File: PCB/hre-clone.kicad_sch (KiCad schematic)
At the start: 23 parts, among them SW1 SW_DIP_x04, U1 74LS258, U10 MC6845, U11 MC6845, U12 DIL14, U13 7402, U2 74LS174, U3 74LS257, U4 74LS244, U5 2716, U6 2716, U7 74LS05, U8 74LS155, U9 74LS257

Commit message: Re-organize file, remove backup files, update readme
A little more organization always helps!
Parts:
- U1, U2, U3, U8, U9: footprint Housings_DIP:DIP-16_W7.62mm_LongPads -> Package_DIP:DIP-16_W7.62mm
- U12, U13, U7: footprint Housings_DIP:DIP-14_W7.62mm_LongPads -> Package_DIP:DIP-14_W7.62mm
- U4: footprint Housings_DIP:DIP-20_W7.62mm_LongPads -> Package_DIP:DIP-20_W7.62mm
- U5, U6: footprint Housings_DIP:DIP-24_W15.24mm_LongPads -> Package_DIP:DIP-24_W15.24mm
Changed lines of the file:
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@@
 			)
 		)
-		(property "Footprint" "Housings_DIP:DIP-16_W7.62mm_LongPads"
+		(property "Footprint" "Package_DIP:DIP-16_W7.62mm"
 			(at 128.27 61.214 0)
 			(hide yes)
@@
 			)
 		)
-		(property "Footprint" "Housings_DIP:DIP-16_W7.62mm_LongPads"
+		(property "Footprint" "Package_DIP:DIP-16_W7.62mm"
 			(at 189.23 58.166 0)
 			(hide yes)
@@
 			)
 		)
-		(property "Footprint" "Housings_DIP:DIP-16_W7.62mm_LongPads"
+		(property "Footprint" "Package_DIP:DIP-16_W7.62mm"
 			(at 260.604 58.674 0)
 			(hide yes)
@@
 			)
 		)
-		(property "Footprint" "Housings_DIP:DIP-20_W7.62mm_LongPads"
+		(property "Footprint" "Package_DIP:DIP-20_W7.62mm"
 			(at 48.514 58.928 0)
 			(hide yes)
@@
 			)
 		)
-		(property "Footprint" "Housings_DIP:DIP-24_W15.24mm_LongPads"
+		(property "Footprint" "Package_DIP:DIP-24_W15.24mm"
 			(at 80.518 109.22 0)
 			(hide yes)
@@
 			)
 		)
-		(property "Footprint" "Housings_DIP:DIP-24_W15.24mm_LongPads"
+		(property "Footprint" "Package_DIP:DIP-24_W15.24mm"
 			(at 144.526 108.458 0)
 			(hide yes)
@@
 			)
 		)
-		(property "Footprint" "Housings_DIP:DIP-14_W7.62mm_LongPads"
+		(property "Footprint" "Package_DIP:DIP-14_W7.62mm"
 			(at 190.754 91.186 0)
 			(hide yes)
@@
 			)
 		)
-		(property "Footprint" "Housings_DIP:DIP-14_W7.62mm_LongPads"
+		(property "Footprint" "Package_DIP:DIP-14_W7.62mm"
 			(at 190.754 101.346 0)
 			(hide yes)
@@
 			)
 		)
-		(property "Footprint" "Housings_DIP:DIP-14_W7.62mm_LongPads"
+		(property "Footprint" "Package_DIP:DIP-14_W7.62mm"
 			(at 190.754 111.506 0)
 			(hide yes)
@@
 			)
 		)
-		(property "Footprint" "Housings_DIP:DIP-14_W7.62mm_LongPads"
+		(property "Footprint" "Package_DIP:DIP-14_W7.62mm"
 			(at 190.754 121.666 0)
 			(hide yes)
@@
 			)
 		)
-		(property "Footprint" "Housings_DIP:DIP-14_W7.62mm_LongPads"
+		(property "Footprint" "Package_DIP:DIP-14_W7.62mm"
 			(at 190.754 130.556 0)
 			(hide yes)
@@
 			)
 		)
-		(property "Footprint" "Housings_DIP:DIP-14_W7.62mm_LongPads"
+		(property "Footprint" "Package_DIP:DIP-14_W7.62mm"
 			(at 190.754 139.446 0)
 			(hide yes)
@@
 			)
 		)
-		(property "Footprint" "Housings_DIP:DIP-16_W7.62mm_LongPads"
+		(property "Footprint" "Package_DIP:DIP-16_W7.62mm"
 			(at 262.128 95.504 0)
 			(hide yes)
@@
 			)
 		)
-		(property "Footprint" "Housings_DIP:DIP-16_W7.62mm_LongPads"
+		(property "Footprint" "Package_DIP:DIP-16_W7.62mm"
 			(at 256.794 129.286 0)
 			(hide yes)
@@
 			)
 		)
-		(property "Footprint" "Housings_DIP:DIP-14_W7.62mm_LongPads"
+		(property "Footprint" "Package_DIP:DIP-14_W7.62mm"
 			(at 251.46 159.258 0)
 			(hide yes)
@@
 			)
 		)
-		(property "Footprint" "Housings_DIP:DIP-14_W7.62mm_LongPads"
+		(property "Footprint" "Package_DIP:DIP-14_W7.62mm"
 			(at 251.46 171.958 0)
 			(hide yes)
@@
 			)
 		)
-		(property "Footprint" "Housings_DIP:DIP-14_W7.62mm_LongPads"
+		(property "Footprint" "Package_DIP:DIP-14_W7.62mm"
 			(at 251.714 186.944 0)
 			(hide yes)
@@
 			)
 		)
-		(property "Footprint" "Housings_DIP:DIP-14_W7.62mm_LongPads"
+		(property "Footprint" "Package_DIP:DIP-14_W7.62mm"
 			(at 251.714 200.914 0)
 			(hide yes)
@@
 			)
 		)
-		(property "Footprint" "Housings_DIP:DIP-14_W7.62mm_LongPads"
+		(property "Footprint" "Package_DIP:DIP-14_W7.62mm"
 			(at 189.23 181.102 0)
 			(hide yes)

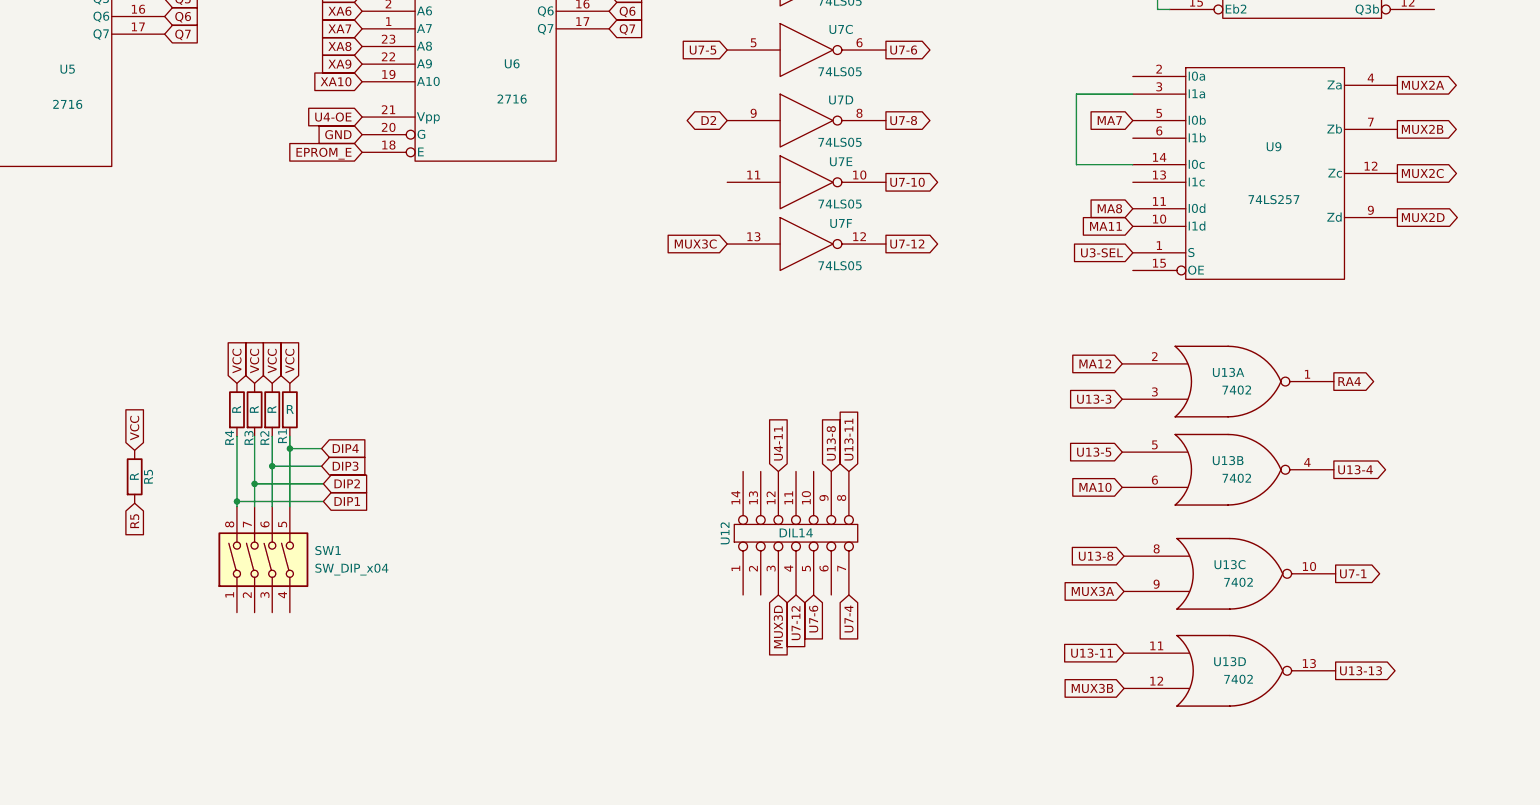
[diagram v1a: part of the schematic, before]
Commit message: Some additional PCB fixes
Getting closer to complete routing. Still some traces under chips that can not be determined.
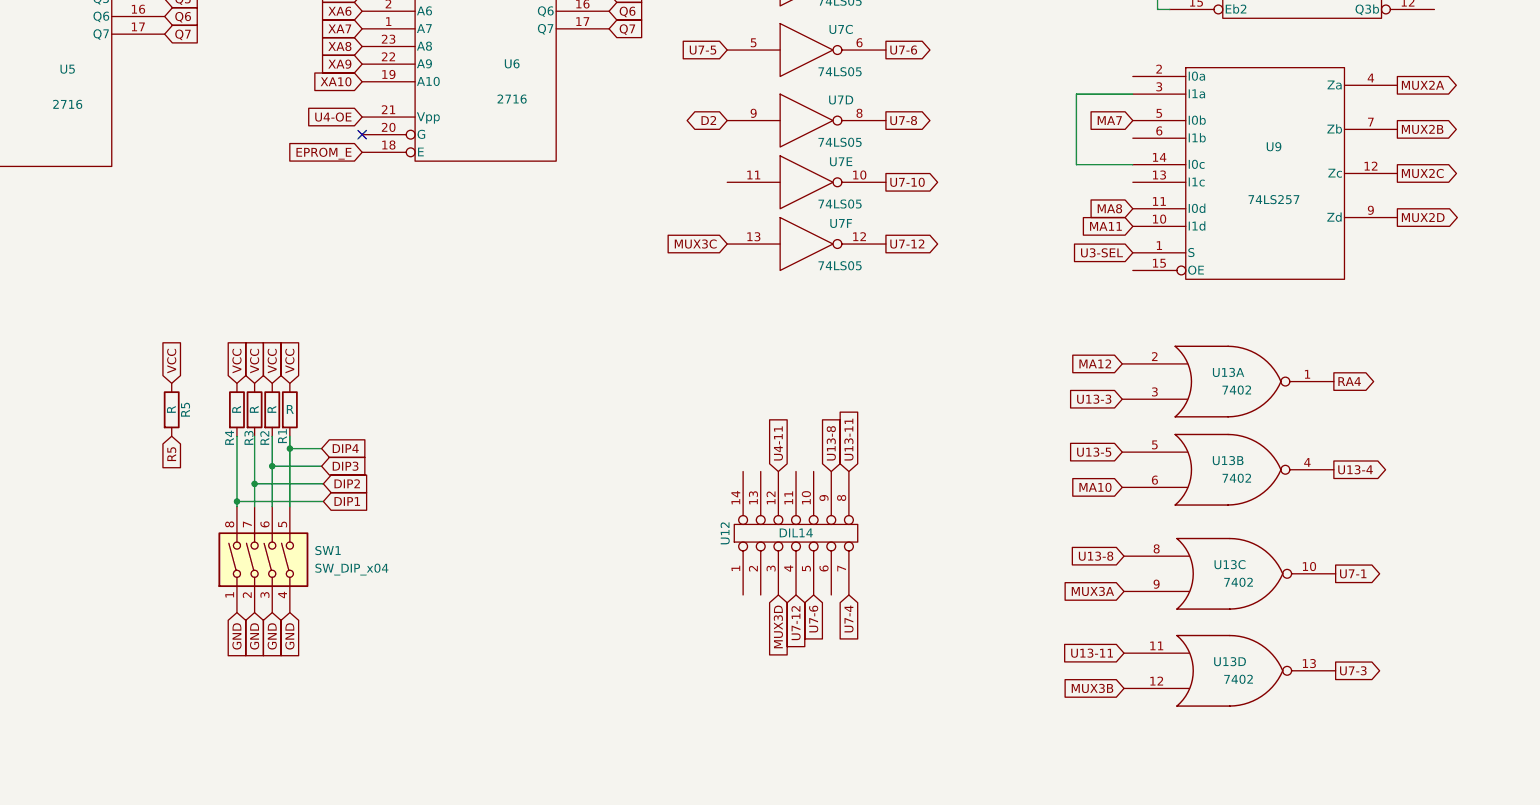
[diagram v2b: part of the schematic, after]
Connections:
- net U13-13 is gone; now on net U7-3: U13.13
- net GND: now also SW1.1, SW1.2, SW1.3, SW1.4; no longer U6.20 (G)
- no-connect marks 0 -> 1
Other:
- moved on the sheet: R5
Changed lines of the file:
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@@
 		(color 0 0 0 0)
 	)
+	(no_connect
+		(at 126.746 123.698)
+	)
 	(wire
 		(pts
@@
 		)
 	)
-	(global_label "U13-13"
+	(global_label "U7-3"
 		(shape output)
 		(at 266.954 200.914 0)
@@
 		)
 		(property "Intersheetrefs" "${INTERSHEET_REFS}"
-			(at 277.0259 200.914 0)
+			(at 274.6069 200.914 0)
 			(hide yes)
 			(show_name no)
@@
 		)
 	)
+	(global_label "GND"
+		(shape input)
+		(at 111.252 192.532 270)
+		(fields_autoplaced yes)
+		(effects
+			(font
+				(size 1.27 1.27)
+			)
+			(justify right)
+		)
+		(property "Intersheetrefs" "${INTERSHEET_REFS}"
+			(at 111.252 198.7335 90)
+			(hide yes)
+			(show_name no)
+			(do_not_autoplace no)
+			(effects
+				(font
+					(size 1.27 1.27)
+				)
+				(justify right)
+			)
+		)
+	)
 	(global_label "D2"
 		(shape bidirectional)
@@
 		)
 	)
+	(global_label "GND"
+		(shape input)
+		(at 113.792 192.532 270)
+		(fields_autoplaced yes)
+		(effects
+			(font
+				(size 1.27 1.27)
+			)
+			(justify right)
+		)
+		(property "Intersheetrefs" "${INTERSHEET_REFS}"
+			(at 113.792 198.7335 90)
+			(hide yes)
+			(show_name no)
+			(do_not_autoplace no)
+			(effects
+				(font
+					(size 1.27 1.27)
+				)
+				(justify right)
+			)
+		)
+	)
 	(global_label "MUX3D"
 		(shape output)
@@
 		)
 	)
+	(global_label "GND"
+		(shape input)
+		(at 116.332 192.532 270)
+		(fields_autoplaced yes)
+		(effects
+			(font
+				(size 1.27 1.27)
+			)
+			(justify right)
+		)
+		(property "Intersheetrefs" "${INTERSHEET_REFS}"
+			(at 116.332 198.7335 90)
+			(hide yes)
+			(show_name no)
+			(do_not_autoplace no)
+			(effects
+				(font
+					(size 1.27 1.27)
+				)
+				(justify right)
+			)
+		)
+	)
 	(global_label "MUX1B"
 		(shape input)
@@
 	(global_label "VCC"
 		(shape input)
-		(at 93.98 169.164 90)
+		(at 99.314 159.512 90)
 		(fields_autoplaced yes)
 		(effects
@@
 		)
 		(property "Intersheetrefs" "${INTERSHEET_REFS}"
-			(at 93.98 163.2044 90)
+			(at 99.314 153.5524 90)
 			(hide yes)
 			(show_name no)
@@
 	(global_label "R5"
 		(shape input)
-		(at 93.98 176.784 270)
+		(at 99.314 167.132 270)
 		(fields_autoplaced yes)
 		(effects
@@
 		)
 		(property "Intersheetrefs" "${INTERSHEET_REFS}"
-			(at 93.98 181.5945 90)
+			(at 99.314 171.9425 90)
 			(hide yes)
 			(show_name no)
@@
 		)
 	)
-	(global_label "GND"
-		(shape input)
-		(at 126.746 123.698 180)
-		(fields_autoplaced yes)
-		(effects
-			(font
-				(size 1.27 1.27)
-			)
-			(justify right)
-		)
-		(property "Intersheetrefs" "${INTERSHEET_REFS}"
-			(at 120.5445 123.698 0)
-			(hide yes)
-			(show_name no)
-			(do_not_autoplace no)
-			(effects
-				(font
-					(size 1.27 1.27)
-				)
-				(justify right)
-			)
-		)
-	)
 	(global_label "RA2"
 		(shape input)
@@
 		)
 	)
+	(global_label "GND"
+		(shape input)
+		(at 108.712 192.532 270)
+		(fields_autoplaced yes)
+		(effects
+			(font
+				(size 1.27 1.27)
+			)
+			(justify right)
+		)
+		(property "Intersheetrefs" "${INTERSHEET_REFS}"
+			(at 108.712 198.7335 90)
+			(hide yes)
+			(show_name no)
+			(do_not_autoplace no)
+			(effects
+				(font
+					(size 1.27 1.27)
+				)
+				(justify right)
+			)
+		)
+	)
 	(global_label "D1"
 		(shape bidirectional)
@@
 	(symbol
 		(lib_id "Device:R")
-		(at 93.98 172.974 0)
+		(at 99.314 163.322 0)
 		(unit 1)
 		(body_style 1)
@@
 		(dnp no)
 		(property "Reference" "R5"
-			(at 96.012 172.974 90)
+			(at 101.346 163.322 90)
 			(show_name no)
 			(do_not_autoplace no)
@@
 		)
 		(property "Value" "R"
-			(at 93.98 172.974 90)
+			(at 99.314 163.322 90)
 			(show_name no)
 			(do_not_autoplace no)
@@
 		)
 		(property "Footprint" "Resistor_THT:R_Axial_DIN0309_L9.0mm_D3.2mm_P12.70mm_Horizontal"
-			(at 92.202 172.974 90)
+			(at 97.536 163.322 90)
 			(hide yes)
 			(show_name no)
@@
 		)
 		(property "Datasheet" ""
-			(at 93.98 172.974 0)
+			(at 99.314 163.322 0)
 			(show_name no)
 			(do_not_autoplace no)
@@
 		)
 		(property "Description" ""
-			(at 93.98 172.974 0)
+			(at 99.314 163.322 0)
 			(show_name no)
 			(do_not_autoplace no)

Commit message: Updated schematics and routing
There are now zero unrouted connections, but a few remaining connections missing under the chips. Added a picture of the traces under the CRTC chip.
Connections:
- net U13-4 is gone; now on an unnamed net: U13.4
- net U13-5 is gone; now on net MA10: U13.5
- net U3-11 is gone; now on net RA2: U3.11 (I0d)
- net U3-13 is gone; now on net MA8: U3.13 (I1c)
- net U3-2 is gone; now on net RA0: U3.2 (I0a)
- net U3-5 is gone; now on net RA1: U3.5 (I0b)
- net U4-12 is gone; now on net Q0: U4.12 (O3a)
- net U4-14 is gone; now on net Q2: U4.14 (O2a)
- net U4-2 is gone; now on net XA7: U4.2 (I0a)
- net U4-3 is gone; now on net Q5: U4.3 (O3b)
- net U4-7 is gone; now on net Q1: U4.7 (O1b)
- net U4-8 is gone; now on net XA5: U4.8 (I3a)
- net U4-9 is gone; now on net XA3: U4.9 (O0b)
- net U4-OE is gone; now on net U3-SEL: U4.1 (OEa), U4.19 (OEb), U5.21 (Vpp), U6.21 (Vpp)
- net U7-8 is gone; now on net R5: U7.8
- net D3: no longer U2.11 (D3)
- net D4: now also U2.11 (D3); no longer U2.13 (D4)
- net D5: now also U2.13 (D4); no longer U2.14 (D5)
- net DIP1: now also U1.11 (I0d)
- net DIP2: now also U1.5 (I0b)
- net DIP3: now also U1.14 (I0c)
- net GND: now also U8.14 (Eb1), U8.15 (Eb2), U9.15 (OE)
- net MA6: now also U9.2 (I0a)
- net MA9: now also U9.6 (I1b); no longer U10.13 (MA9)
- net MUX2A: now also U10.13 (MA9)
- net RA4: no longer U11.34 (RA4)
- net U2-CP: no longer U2.9 (Cp)
- net U2-MR: no longer U2.1 (~{Mr})
- net ~{CS}: no longer U11.25 (~{CS})
- net U8-13: now reaches U8.13 (A0)
- net U8-13: now also U12.6
- net LATCH: now reaches U8.4 (Q3a)
- net LATCH: now also U2.9 (Cp)
- net RS renamed A0
- net A0: now also U2.14 (D5)
- net U13-3: no longer names the net of U13.3
- net U8-9 renamed ~{CRTC_CS}
- net ~{CRTC_CS}: now also U11.25 (~{CS})
- no-connect marks 1 -> 2
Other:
- note added: "$E880-$E881"
- note added: "$E882-$E883"
- note added: "8296 HRE Clone"
- note added: "Address Translation ??? ============ U10 U11 U11 TEXT HIRES MA5 MA5 RA0 MA6 MA6 RA1 MA7 MA7 RA2 MA8 MA8 MA5 MA9 MA9 MA6 MA10 MA10 MA7 MA11 MA11 MA8 MA12 MA12 MA9"
- note added: "CHAR ROM"
- note added: "CHAR ROM HEADER"
- note added: "CREATED: 2016-04-22 UPDATED: 2026-10-11"
- note added: "CRTC HEADER"
- note added: "DECODER"
- note added: "Emulates HSG Board"
- note added: "LATCH"
- note added: "MULTIPLEXERS"
- note added: "Missing Q2 and Q7"
- note added: "This is a clone of the Commodore 8296 High-Res Emulator (HRE) board. The HRE is a board plus firmware that emulates the Commodore High-Speed Grahic (HSG) board which contains a Thomson EF9365/EF9366 Video Display Processor (VDP). The HRE firmware implements the same BASIC commands as the HSG but does the drawing with the 6502 processor rather than the VDP chip."
- note added: "XCVR"
- note removed: "CREATED: 2016-04-22 UPDATED: 2026-10-10"
- note removed: "CRTC SOCKET"
- note removed: "High Res Emulator of HRG Board"
- note removed: "PET HRE Clone"
- note removed: "This is a clone of the Commodore 8296 High-Res Emulator (HRE) board. The HRE is a board plus firmware that emulates the Commodore High-Speed Grahic (HSG) board which contains a Thomson EF Video Display Processor (VDP). The HRE firmware implements the same BASIC commands as the HSG but does the drawing with the 6502 processor rather than the VDP chip."
- moved on the sheet: R1, R2, R3, R4, R5, SW1, U1, U10, U11, U12, U13A, U13B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

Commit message: Routing complete
Thanks to Andy Grady for corrections for some traces. DRC check ok. Updated many global labels, moved around some symbols, updated board text etc
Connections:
- net U3-SEL is gone; now on net MUX2SEL: U3.1 (S), U4.1 (OEa), U4.19 (OEb), U5.21 (Vpp), U6.21 (Vpp), U9.1 (S)
- net U4-17 is gone; now on net XA8: U4.17 (I3b)
- net U4-6 is gone; now on net XA5: U4.6 (I2a)
- net D7: now also U2.14 (D5)
- net GND: now also U9.13 (I1c)
- net LATCH: now also U8.6 (Q1a); no longer U8.4 (Q3a)
- net MA10: now also U9.6 (I1b)
- net MA9: now also U9.14 (I0c), U9.3 (I1a); no longer U9.6 (I1b)
- net Q7: now also U4.9 (O0b)
- net XA3: now also U4.8 (I3a); no longer U4.9 (O0b)
- net XA5: no longer U4.8 (I3a)
- net ~{RESET}: now also U2.1 (~{Mr})
- net RIBBON-11: now reaches U12.11
- net RIBBON-11: now also U8.13 (A0)
- net A0 renamed RS
- net RS: no longer U2.14 (D5)
- net EPROM_E renamed XA11
- net MA12 renamed MUX2SEL
- net MUX3C: no longer names the net of U1.12 (Zc), U7.13
- net R5: no longer names the net of R5.2, U2.6 (D2), U7.8
- net U1-10 renamed LATCH1
- net U1-3 renamed LATCH4
- net U1-6 renamed LATCH3
- net U1-SEL renamed MUX1SEL
- net U13-11 renamed RIBBON-8
- net U13-8 renamed RIBBON-9
- net U2-2 renamed LATCH0
- net U4-11 renamed RIBBON-12
- net U7-1: no longer names the net of U13.10, U7.1
- net U7-10: no longer names the net of U7.10
- net U7-12 renamed ~{MUX3C}
- net U7-3: no longer names the net of U13.13, U7.3
- net U7-4 renamed RIBBON-7
- net U7-5: no longer names the net of U2.7 (Q2), U7.5
- net U7-6 renamed ~{LATCH2}
- net U8-13: no longer names the net of U12.6
- net U8-13: no longer U8.13 (A0)
- no-connect marks 2 -> 16
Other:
- note added: "/CS"
- note added: "A11"
- note added: "Address Translation =================== U10 U11 U11 --- --- --- MODE: TEXT HIRES MA5 MA5 RA0 MA6 MA6 RA1 MA7 MA7 RA2 MA8 MA8 MA5 MA9 MA9 MA6 MA10 MA10 MA7 MA11 MA11 MA8 MA12 MA12 MA9"
- note added: "CREATED: 2016-04-22 UPDATED: 2026-10-12"
- note added: "DIP SWITCHES"
- note added: "RIBBON CABLE"
- note added: "SPARES"
- note added: "The CHR ROM socket supports a 2316 (2K) or 2332 (4K). Normally it is only 2K except for SuperPET or some DIN machines. * Pin 18 is used as A11. * Pin 21 is used as /CS"
- note added: "This is a clone of the Commodore 8296 High-Res Emulator (HRE) board. The HRE is a board plus firmware that emulates the Commodore High-Speed Grahic (HSG) board which contains a Thomson EF9365/EF9366 Video Display Processor (VDP). The HRE firmware implements the same BASIC commands as the HSG but does the drawing with the 6502 processor rather than the VDP chip. Thanks to Andy Grady for sorting ou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"
- note added: "To CHR ROM"
- note removed: "Address Translation ??? ============ U10 U11 U11 TEXT HIRES MA5 MA5 RA0 MA6 MA6 RA1 MA7 MA7 RA2 MA8 MA8 MA5 MA9 MA9 MA6 MA10 MA10 MA7 MA11 MA11 MA8 MA12 MA12 MA9"
- note removed: "CREATED: 2016-04-22 UPDATED: 2026-10-11"
- note removed: "Missing Q2 and Q7"
- note removed: "This is a clone of the Commodore 8296 High-Res Emulator (HRE) board. The HRE is a board plus firmware that emulates the Commodore High-Speed Grahic (HSG) board which contains a Thomson EF9365/EF9366 Video Display Processor (VDP). The HRE firmware implements the same BASIC commands as the HSG but does the drawing with the 6502 processor rather than the VDP chip."
- moved on the sheet: C1, C2, C3, C4, R1, R2, R3, R4, R5, SW1, U1, U12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
